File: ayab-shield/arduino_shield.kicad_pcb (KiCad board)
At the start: 2 copper layers, 74.1 x 53.3 mm, 35 parts, among them IC1 ULN2803A, IC2 ULN2803A, IC3 MCP2300X/P, IC4 MCP2300X/P, J1 Power, J2 Digital/PWM, J3 Analog, J4 Digital/PWM, X1 KLDX-0202-AC

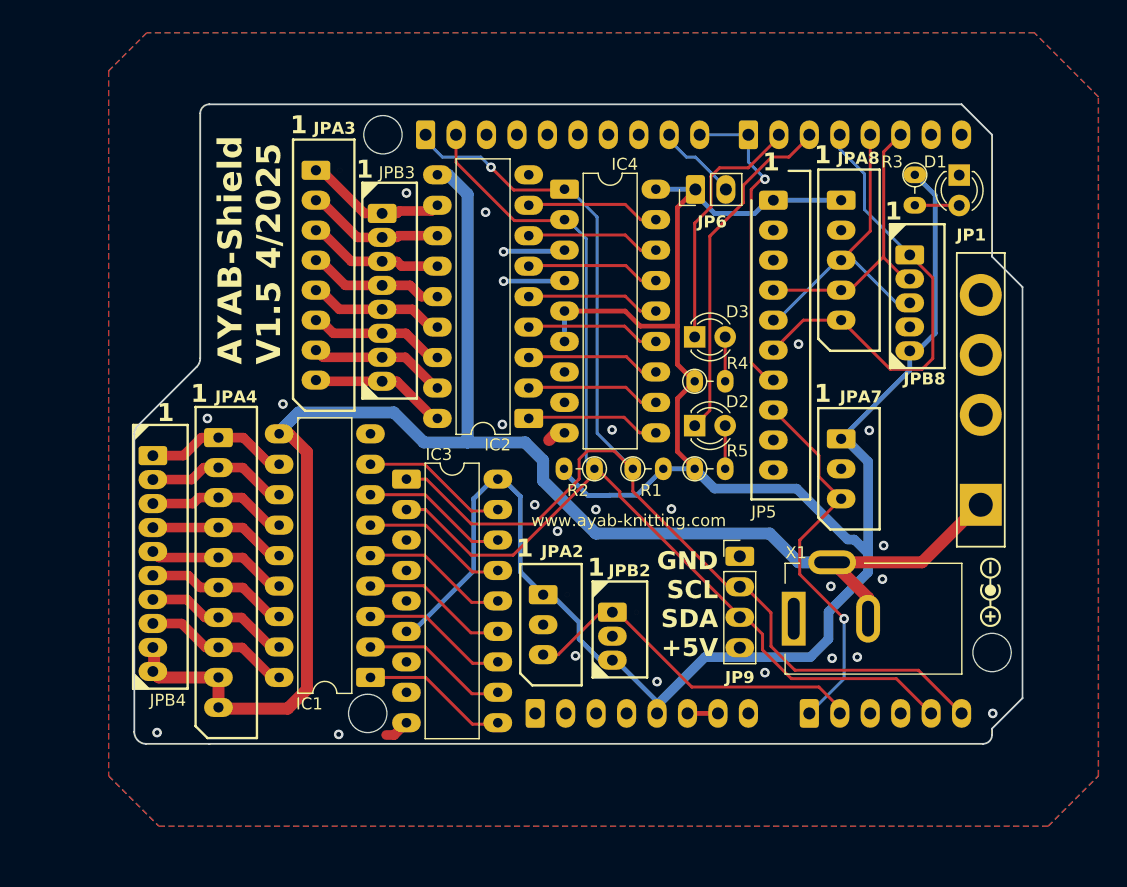
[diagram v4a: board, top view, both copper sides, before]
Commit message: Switch to Hirose connector footprints, extend board 1mm
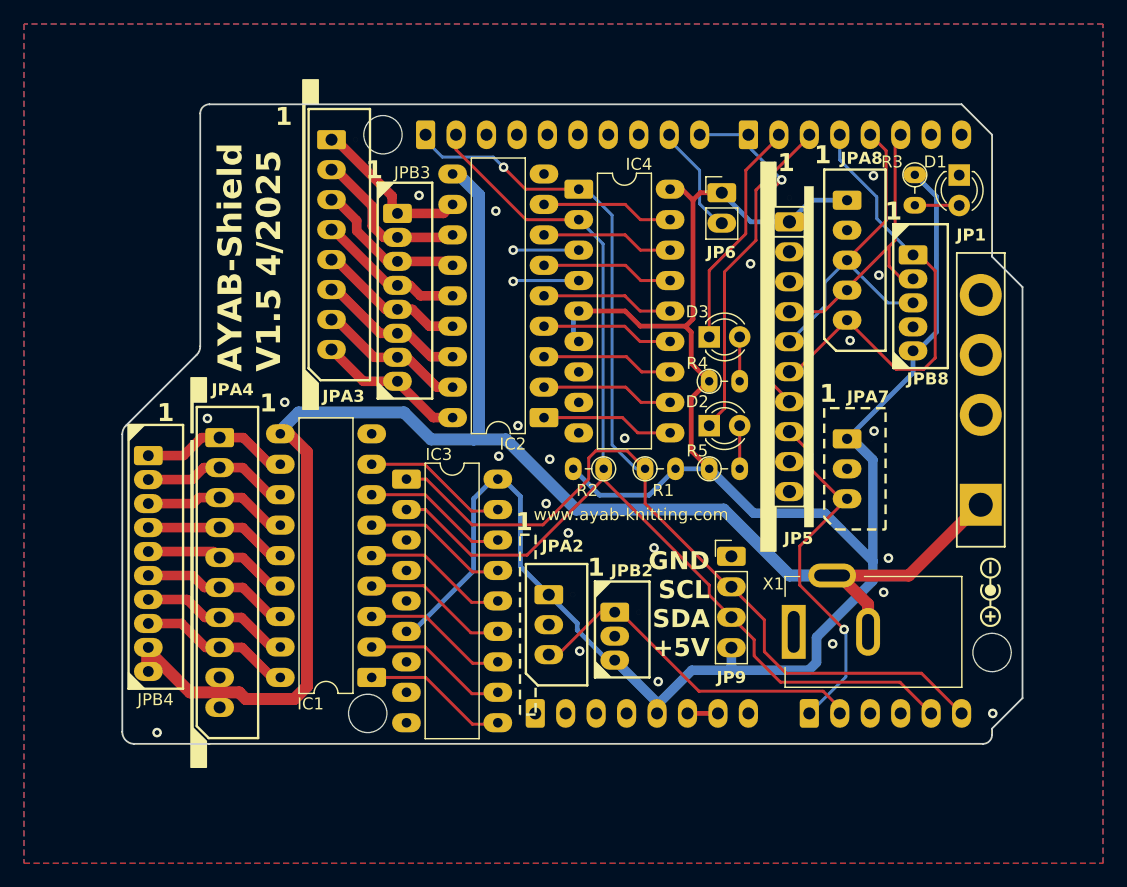
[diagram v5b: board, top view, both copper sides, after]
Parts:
- JP5: footprint ayab-library:SHDR10W70P0X250_1X10_2740X490X590P_LongPads -> ayab-library:HNC2-2.5P-10DS_LongPads
- JPA2: footprint ayab-library:Molex_SPOX_5267-03A_1x03_P2.50mm_Vertical_LongPads -> ayab-library:Molex_0022035035_or_Hirose_HNC2-2.5P-3DS_LongPads_dashed_bar
- JPA3: footprint ayab-library:Molex_SPOX_5267-08A_1x08_P2.50mm_Vertical_LongPads -> ayab-library:Molex_0022035085_or_Hirose_HNC2_2.5P_8DS_LongPads
- JPA4: footprint ayab-library:Molex_SPOX_5267-10A_1x10_P2.50mm_Vertical_LongPads -> ayab-library:Molex_0022035105_or_Hirose_HNC2-2.5P-10DS_LongPads
- JPA7: footprint ayab-library:Molex_SPOX_5267-03A_1x03_P2.50mm_Vertical_LongPads -> ayab-library:Molex_SPOX_5267-03A_1x03_P2.50mm_Vertical_LongPads_dashed_outline
- moved JP5 20.7 mm to (163.8, 86.5), turned to -90 degrees
- moved JPA3 2.86 mm to (125.7, 79.7)
- moved JP6 2.22 mm to (158.2, 84.1), turned to 0 degrees
- moved JPB3 1.28 mm to (131.2, 85.8)
- moved IC2 1.27 mm to (143.4, 102.8)
- moved D2 1.21 mm to (157.2, 103.5)
- moved D3 1.21 mm to (157.2, 96.1)
- moved R4 1.21 mm to (157.2, 99.8)
- moved R5 1.21 mm to (157.2, 107.1)
- moved IC4 1.19 mm to (146.3, 83.8)
- moved X1 1.10 mm to (164.2, 120.7)
- moved R1 1.02 mm to (151.8, 107.1)
- moved R2 0.77 mm to (148.3, 107.1)
- moved JP9 0.70 mm to (159.0, 114.4)
- moved JPA7 0.50 mm to (168.7, 104.6)
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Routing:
- net +15V: track 138.4 -> 142.4 mm
- net GND: track 16.6 -> 13.6 mm
- net /SCL: track 102.9 -> 105.3 mm
- net /BUZZ: track 6.96 -> 9.33 mm
- net Net-(IC2-O7): track 11.5 -> 13.5 mm
- net /LED_GRN: track 21.2 -> 19.3 mm
- net Net-(IC2-O8): track 12.0 -> 13.9 mm
- net /ENC_B: track 26.7 -> 28.5 mm
- net /910_L: track 27.0 -> 28.5 mm
- net /EOL_R: track 31.8 -> 30.3 mm
- net Net-(IC2-O6): track 11.4 -> 12.9 mm
- net /LED_YEL: track 29.1 -> 27.7 mm
- net /SDA: track 93.4 -> 94.6 mm
- net Net-(IC2-O4): track 11.4 -> 12.5 mm
- net Net-(IC2-O3): track 11.4 -> 12.4 mm
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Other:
- board size 74.1 x 53.3 mm -> 75.1 x 53.3 mm

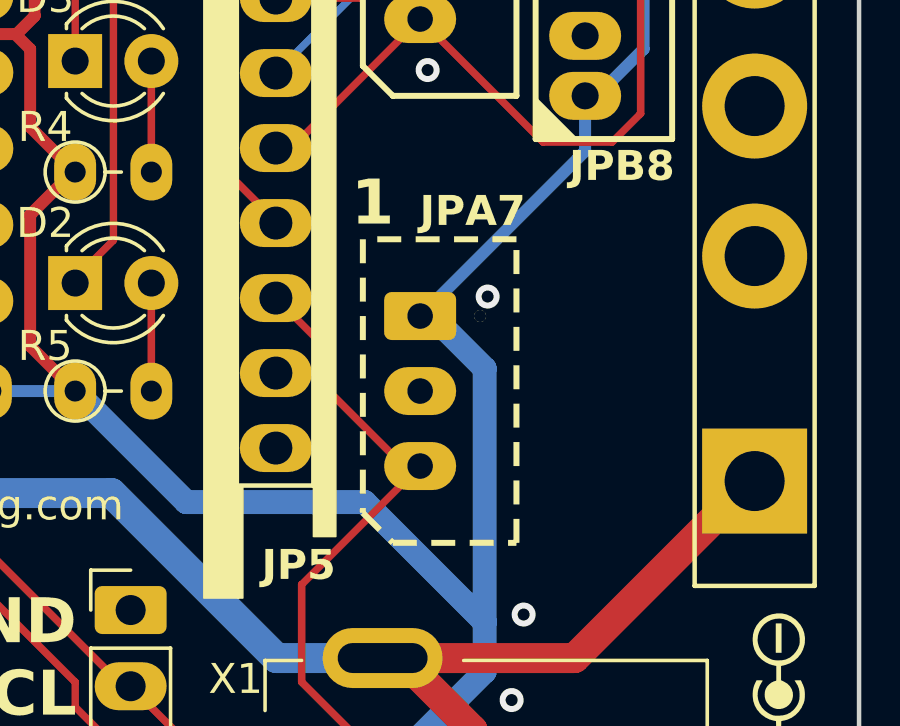
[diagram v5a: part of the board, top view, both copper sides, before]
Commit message: Change footprint for JPA7
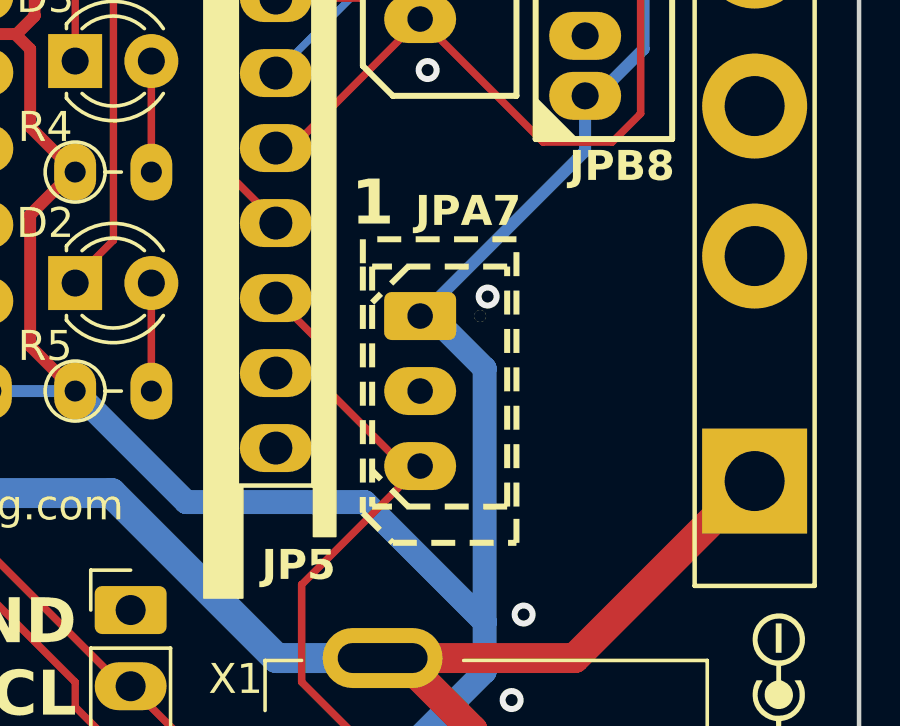
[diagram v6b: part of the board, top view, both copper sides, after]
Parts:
- JPA7: footprint ayab-library:Molex_SPOX_5267-03A_1x03_P2.50mm_Vertical_LongPads_dashed_outline -> ayab-library:Molex_530140310_or_SPOX_5267-03A_1x03_P2.50mm_Vertical_LongPads_dashed_outline_1
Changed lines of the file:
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@@
 			(usegerberadvancedattributes yes)
 			(creategerberjobfile yes)
-			(dashed_line_dash_ratio 12.000000)
-			(dashed_line_gap_ratio 3.000000)
+			(dashed_line_dash_ratio 0.250000)
+			(dashed_line_gap_ratio 0.750000)
 			(svgprecision 6)
 			(plotframeref no)
@@
 		)
 		(model "${KIPRJMOD}/../ayab-library/packages3D/HNC2-2.5P-3DS.step"
+			(hide yes)
 			(offset
 				(xyz 10 2 0)
@@
 		)
 	)
-	(footprint "ayab-library:Molex_SPOX_5267-03A_1x03_P2.50mm_Vertical_LongPads_dashed_outline"
+	(footprint "ayab-library:Molex_530140310_or_SPOX_5267-03A_1x03_P2.50mm_Vertical_LongPads_dashed_outline_1"
 		(layer "F.Cu")
 		(at 168.65 104.6 -90)
@@
 		(tags "connector Molex SPOX vertical")
 		(property "Reference" "JPA7"
-			(at -3.5 -1.75 180)
+			(at -3.5 -1.6 0)
 			(layer "F.SilkS")
 			(effects
@@
 		)
 		(property "Value" "1X3 2.5mm"
-			(at 2.5 3.01 270)
+			(at 2.5 3.01 90)
 			(layer "F.Fab")
 			(effects
@@
 		)
 		(property "Datasheet" ""
-			(at 0 0 270)
+			(at 0 0 90)
 			(layer "F.Fab")
 			(hide yes)
@@
 		)
 		(property "Description" ""
-			(at 0 0 270)
+			(at 0 0 90)
 			(layer "F.Fab")
 			(hide yes)
@@
 		(fp_line
 			(start -2.56 1.91)
+			(end -1.65 1.91)
+			(stroke
+				(width 0.2)
+				(type dash)
+			)
+			(layer "F.SilkS")
+		)
+		(fp_line
+			(start -1.65 1.91)
 			(end 6.56 1.91)
 			(stroke
@@
 		)
 		(fp_line
+			(start -1.65 1.6)
+			(end 6.35 1.6)
+			(stroke
+				(width 0.2)
+				(type dash)
+			)
+			(layer "F.SilkS")
+		)
+		(fp_line
 			(start 7.56 0.91)
 			(end 7.56 -3.21)
@@
 		)
 		(fp_line
+			(start -1.65 0.4)
+			(end -0.45 1.6)
+			(stroke
+				(width 0.2)
+				(type dash)
+			)
+			(layer "F.SilkS")
+		)
+		(fp_line
+			(start 6.35 0.4)
+			(end 5.15 1.6)
+			(stroke
+				(width 0.2)
+				(type dash)
+			)
+			(layer "F.SilkS")
+		)
+		(fp_line
+			(start -1.65 -2.9)
+			(end -1.65 1.6)
+			(stroke
+				(width 0.2)
+				(type dash)
+			)
+			(layer "F.SilkS")
+		)
+		(fp_line
+			(start 6.35 -2.9)
+			(end 6.35 1.6)
+			(stroke
+				(width 0.2)
+				(type dash)
+			)
+			(layer "F.SilkS")
+		)
+		(fp_line
+			(start 6.35 -2.9)
+			(end -1.65 -2.9)
+			(stroke
+				(width 0.2)
+				(type dash)
+			)
+			(layer "F.SilkS")
+		)
+		(fp_line
 			(start -2.56 -3.21)
 			(end -2.56 1.91)
@@
 		)
 		(fp_line
-			(start 7.56 -3.21)
+			(start 6.35 -3.21)
 			(end -2.56 -3.21)
 			(stroke
@@
 			(layer "F.SilkS")
 		)
+		(fp_line
+			(start 7.56 -3.21)
+			(end 6.35 -3.21)
+			(stroke
+				(width 0.2)
+				(type dash)
+			)
+			(layer "F.SilkS")
+		)
 		(fp_circle
 			(center 0 -2)
@@
 		)
 		(fp_text user "${REFERENCE}"
-			(at 2.5 -2.4 270)
+			(at 2.5 -2.4 90)
 			(layer "F.Fab")
 			(effects
@@
 		)
 		(model "${KIPRJMOD}/../ayab-library/packages3D/022035035.stp"
+			(hide yes)
 			(offset
 				(xyz 0 0 9)

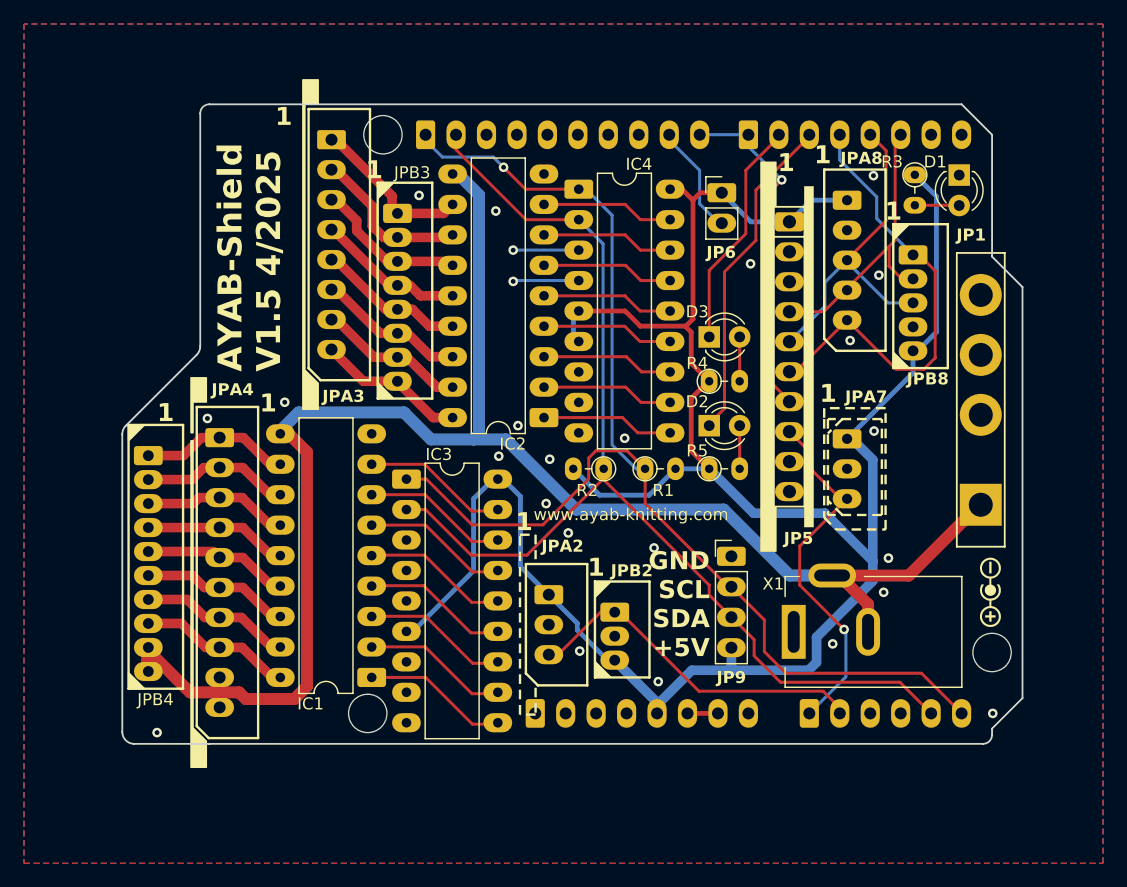
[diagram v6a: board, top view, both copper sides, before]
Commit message: Add ground plane rule zones
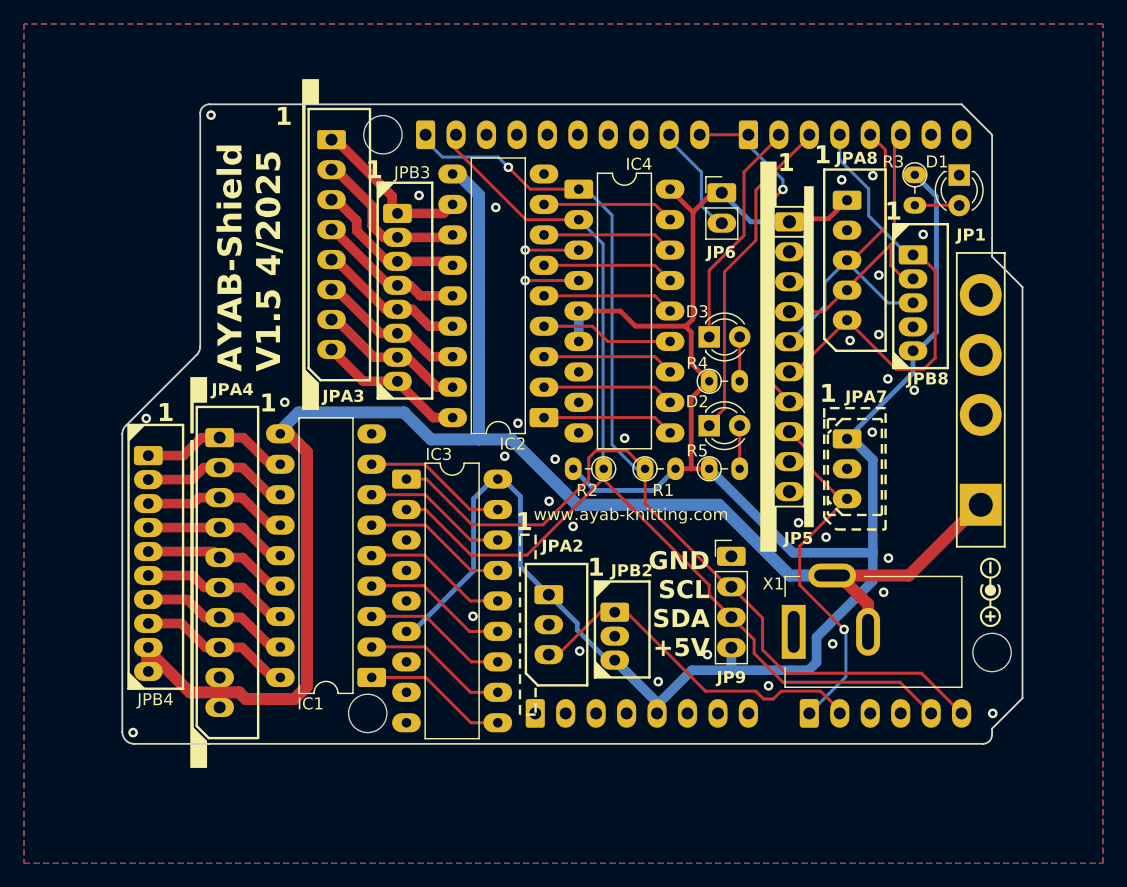
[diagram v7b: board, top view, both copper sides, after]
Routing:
- net GND: track 13.6 -> 8.99 mm, vias 25 -> 34
- net +5V: track 192.3 -> 190.4 mm
